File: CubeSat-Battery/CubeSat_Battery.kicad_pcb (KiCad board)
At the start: 2 copper layers, 92 x 92 mm, 5 parts, among them J1 Conn_01x02_Pin, J2 Conn_01x02_Pin, U1 BatteryPack

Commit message: Mostly fine tuning the boards, also added capacitor for battery ADC
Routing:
- net Vbat_8.4V: track 192.3 -> 193.3 mm

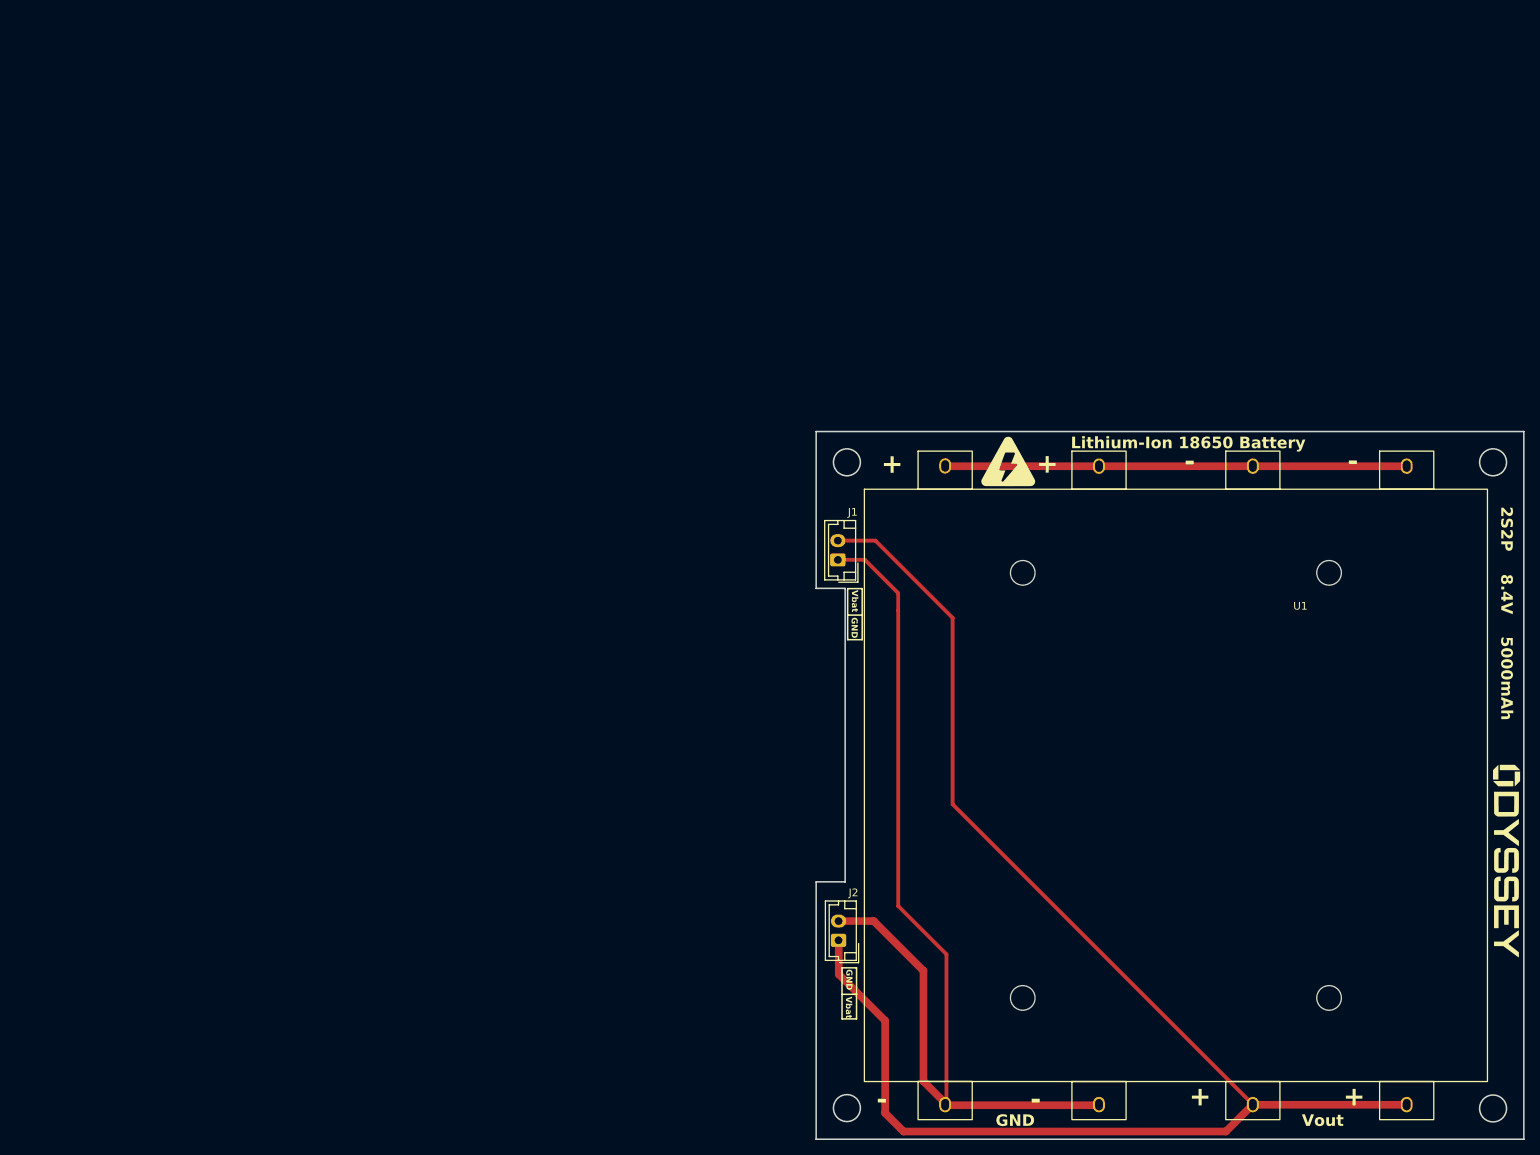
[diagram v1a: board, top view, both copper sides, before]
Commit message: Changing the size of all traces to fit the 1 mm requirement of the draft PCB
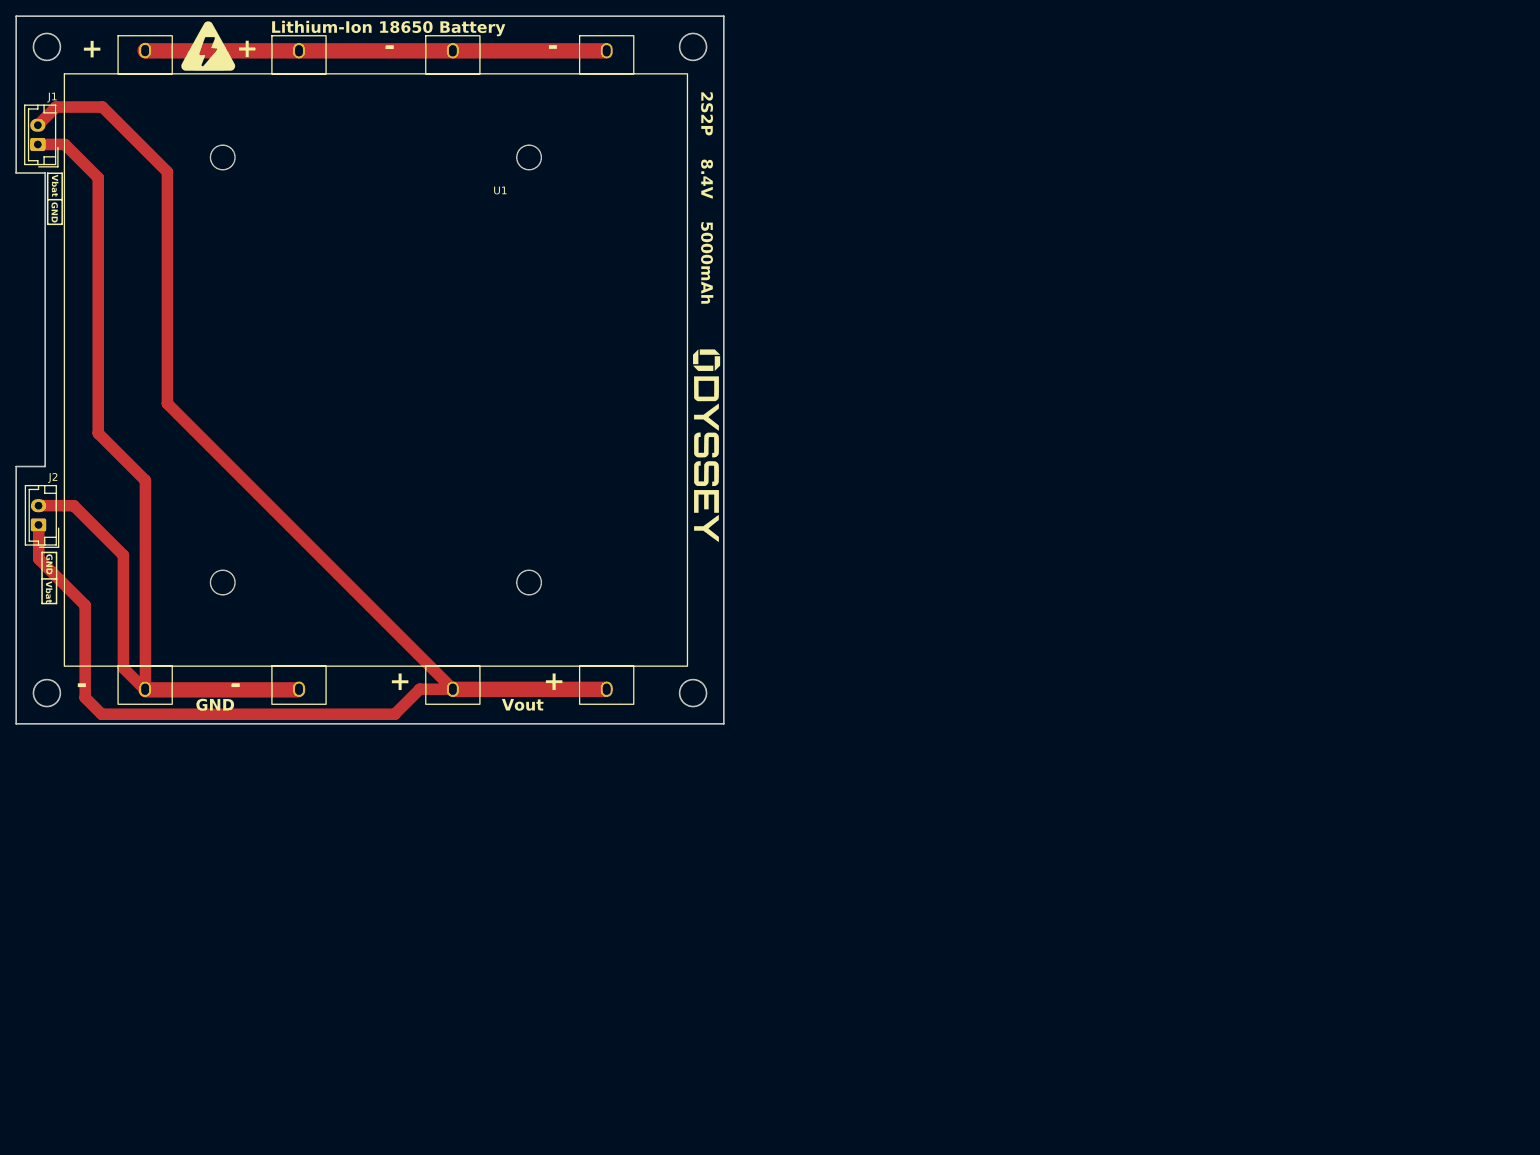
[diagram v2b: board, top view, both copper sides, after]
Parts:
- moved G*** 117.2 mm to (89.8, 55.9)
- moved G*** 117.2 mm to (25.0, 3.89)
- moved J1 117.2 mm to (2.82, 16.7)
- moved J2 117.2 mm to (2.91, 66.1)
- moved U1 117.2 mm to (46.8, 46.0)
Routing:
- net Vbat_8.4V: track 193.3 -> 198.6 mm
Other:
- outline, holes or cut-outs redrawn

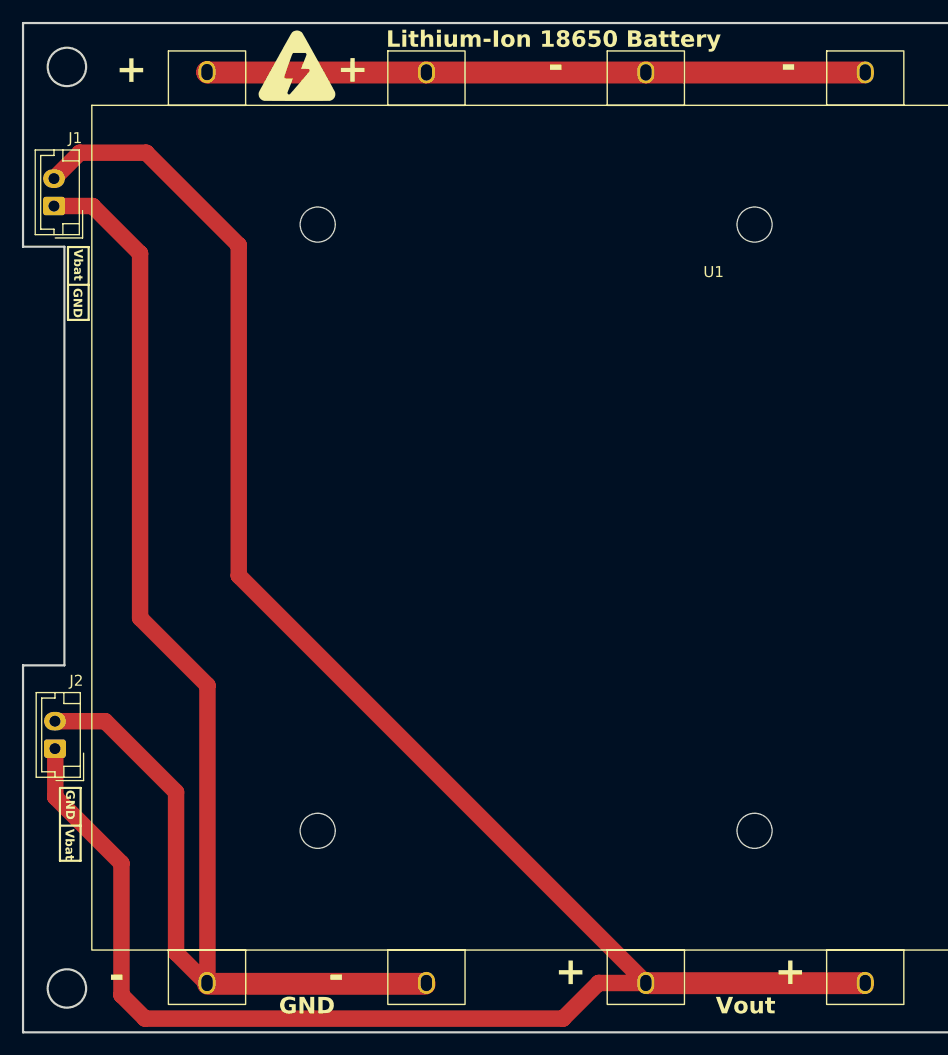
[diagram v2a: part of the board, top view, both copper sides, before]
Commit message: final version of the 3 PCBs, minor size changes for the protoypes
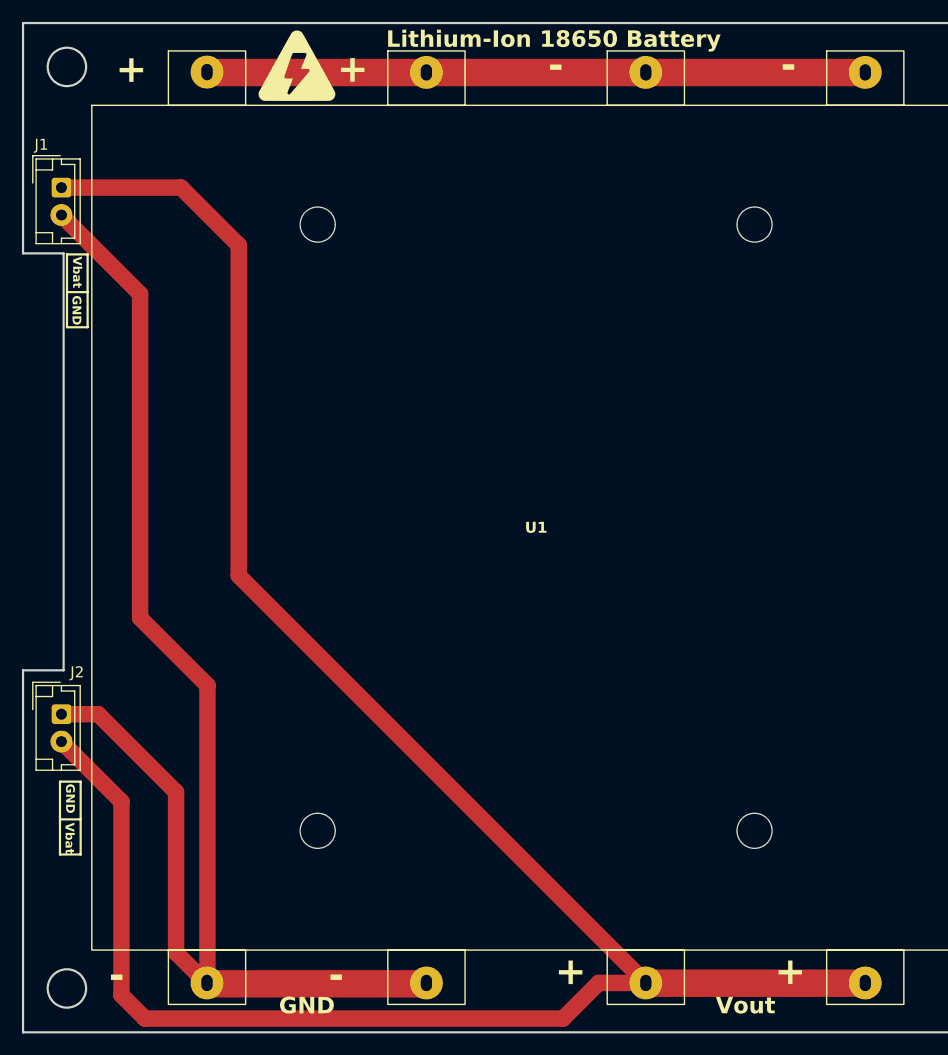
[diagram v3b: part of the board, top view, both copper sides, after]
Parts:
- moved J2 3.19 mm to (3.50, 63.0), turned to -90 degrees
- moved J1 1.81 mm to (3.50, 15.0), turned to -90 degrees
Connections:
- J1 pad 1: GND -> Vbat_8.4V
- J1 pad 2: Vbat_8.4V -> GND
- J2 pad 1: Vbat_8.4V -> GND
- J2 pad 2: GND -> Vbat_8.4V
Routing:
- net GND: track 130.9 -> 127.4 mm
- net Vbat_8.4V: track 198.6 -> 196.0 mm
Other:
- outline, holes or cut-outs redrawn

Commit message: final changes
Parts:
- G*** (x2), J1, J2, U1: moved to B.Cu
- moved G*** 87.5 mm to (2.25, 55.9)
- moved J1 85.5 mm to (89.0, 15.0)
- moved J2 85.5 mm to (89.0, 63.0)
- moved G*** 42.1 mm to (67.0, 3.89), turned to 180 degrees
- moved U1 0.77 mm to (46.0, 46.0), turned to 180 degrees
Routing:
- net GND: track 127.4 -> 128.1 mm
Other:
- outline, holes or cut-outs redrawn

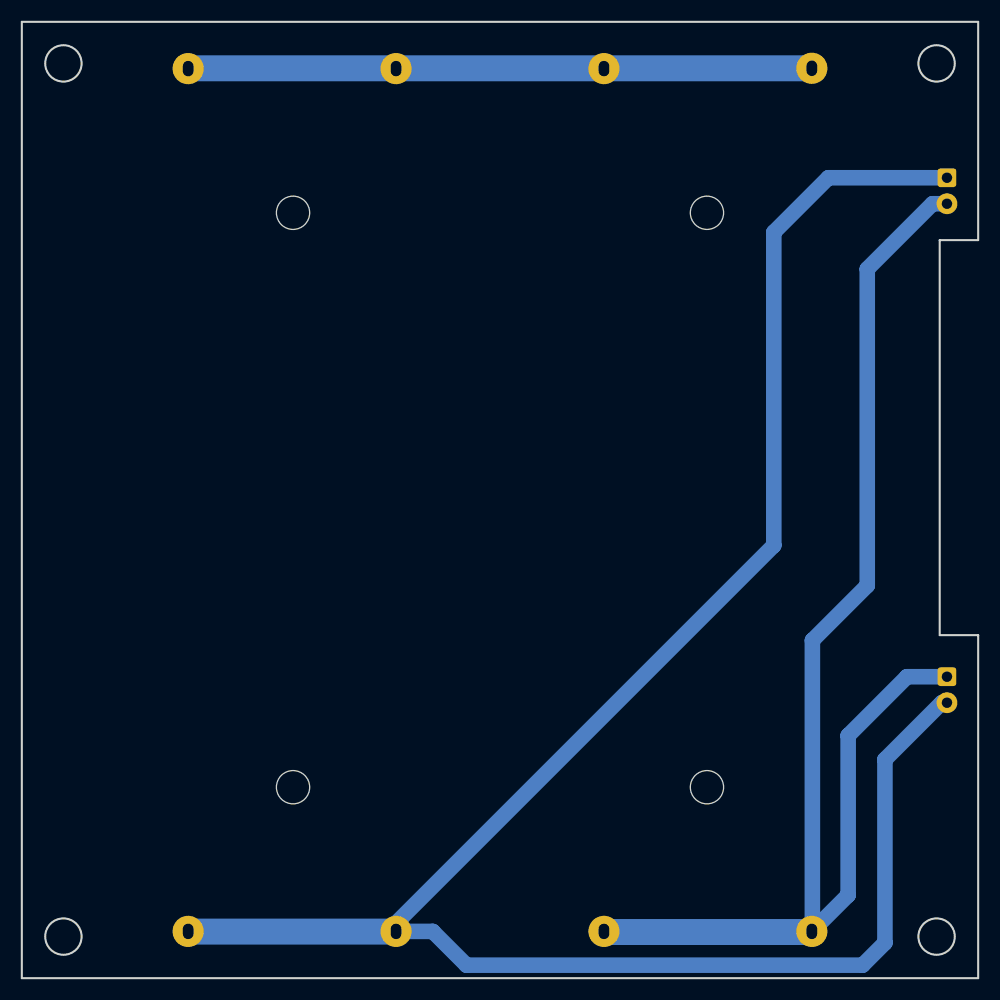
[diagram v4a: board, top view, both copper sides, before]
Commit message: version with the right hole setup
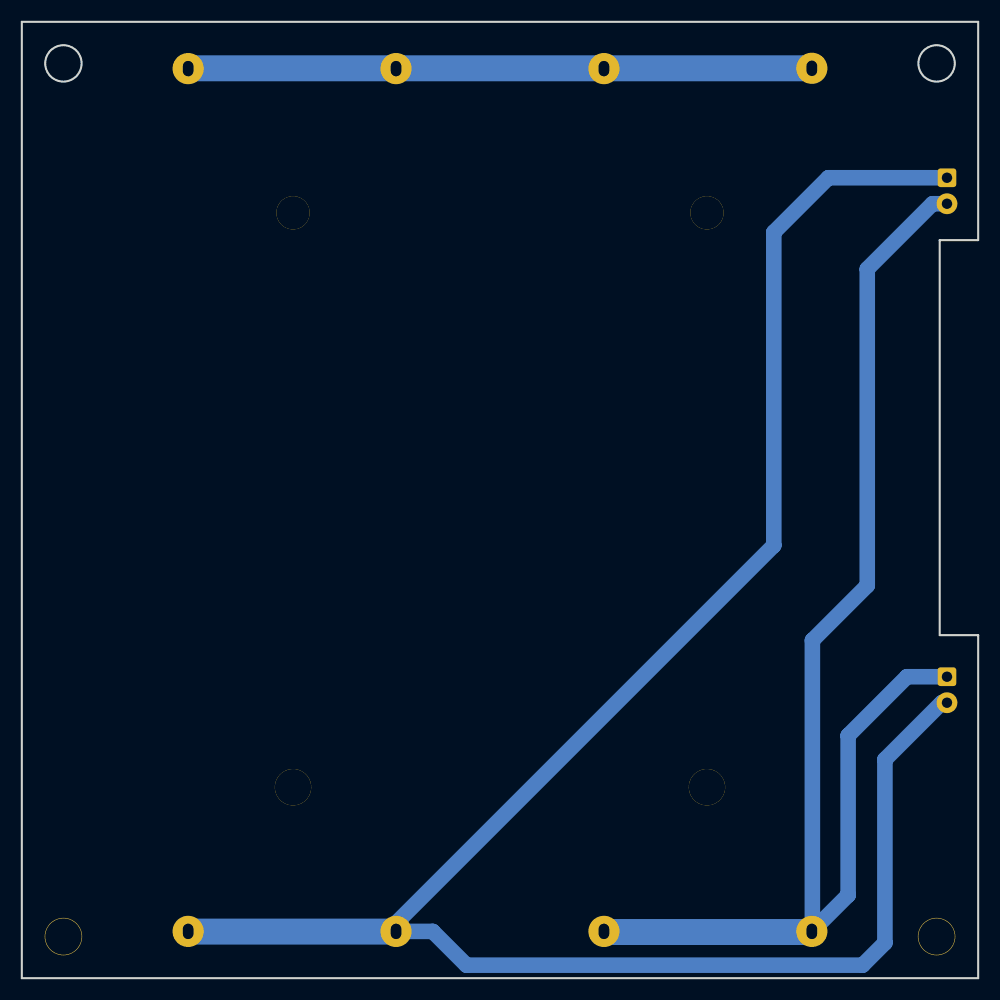
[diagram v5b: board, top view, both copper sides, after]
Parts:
- added ?: , , F.Cu at (89.6, 83.7)
- added ?: , , F.Cu at (-3.53, 3.66)
- added ?: , , F.Cu at (96.8, 4.16)
- added ?: , , F.Cu at (4.01, 88.0)
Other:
- outline, holes or cut-outs redrawn

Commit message: add new drill format
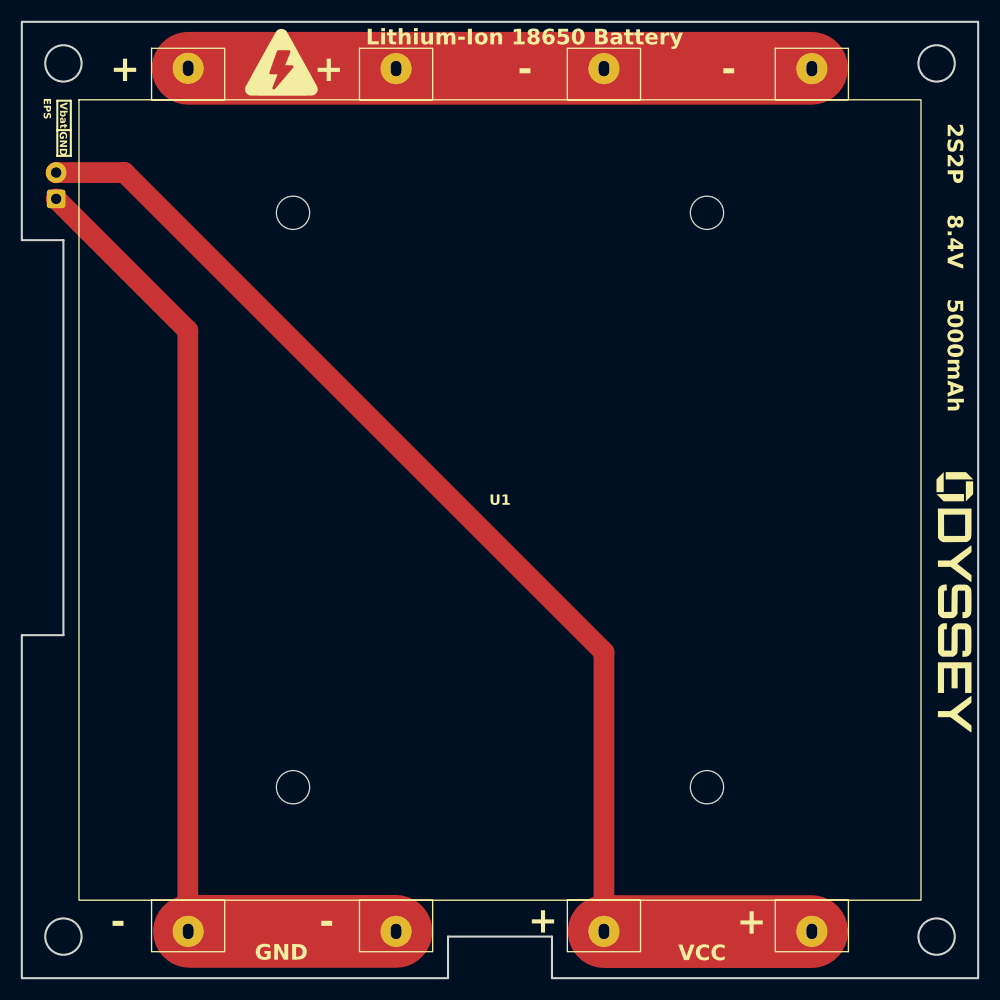
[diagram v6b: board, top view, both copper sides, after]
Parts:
- removed ? (x4): , 
- removed J2: Conn_01x02_Pin, Connector_JST:JST_EH_B2B-EH-A_1x02_P2.50mm_Vertical
- G*** (x2), U1: moved to F.Cu
- moved G*** 87.5 mm to (89.8, 55.9)
- moved J1 85.7 mm to (3.30, 17.0), turned to 90 degrees
- moved G*** 42.1 mm to (25.0, 3.89), turned to 0 degrees
- turned U1 to 0 degrees
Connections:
- J1 pad 1: Vbat_8.4V -> GND
- J1 pad 2: GND -> Vbat_8.4V
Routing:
- net Vbat_8.4V: track 196.3 -> 118.8 mm
- net GND: track 128.1 -> 95.7 mm
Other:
- outline, holes or cut-outs redrawn
- board text added: "EPS"
- board text added: "VCC"
- board text removed: "Vout"
